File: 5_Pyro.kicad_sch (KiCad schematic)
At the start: 24 parts, among them Q601 IRLZ44N, Q602 IRLZ44N, Q603 IRLZ44N, Q604 IRLZ44N, Q605 IRLZ44N, Q606 IRLZ44N, U601 PC817, U602 PC817, U603 PC817, U604 PC817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

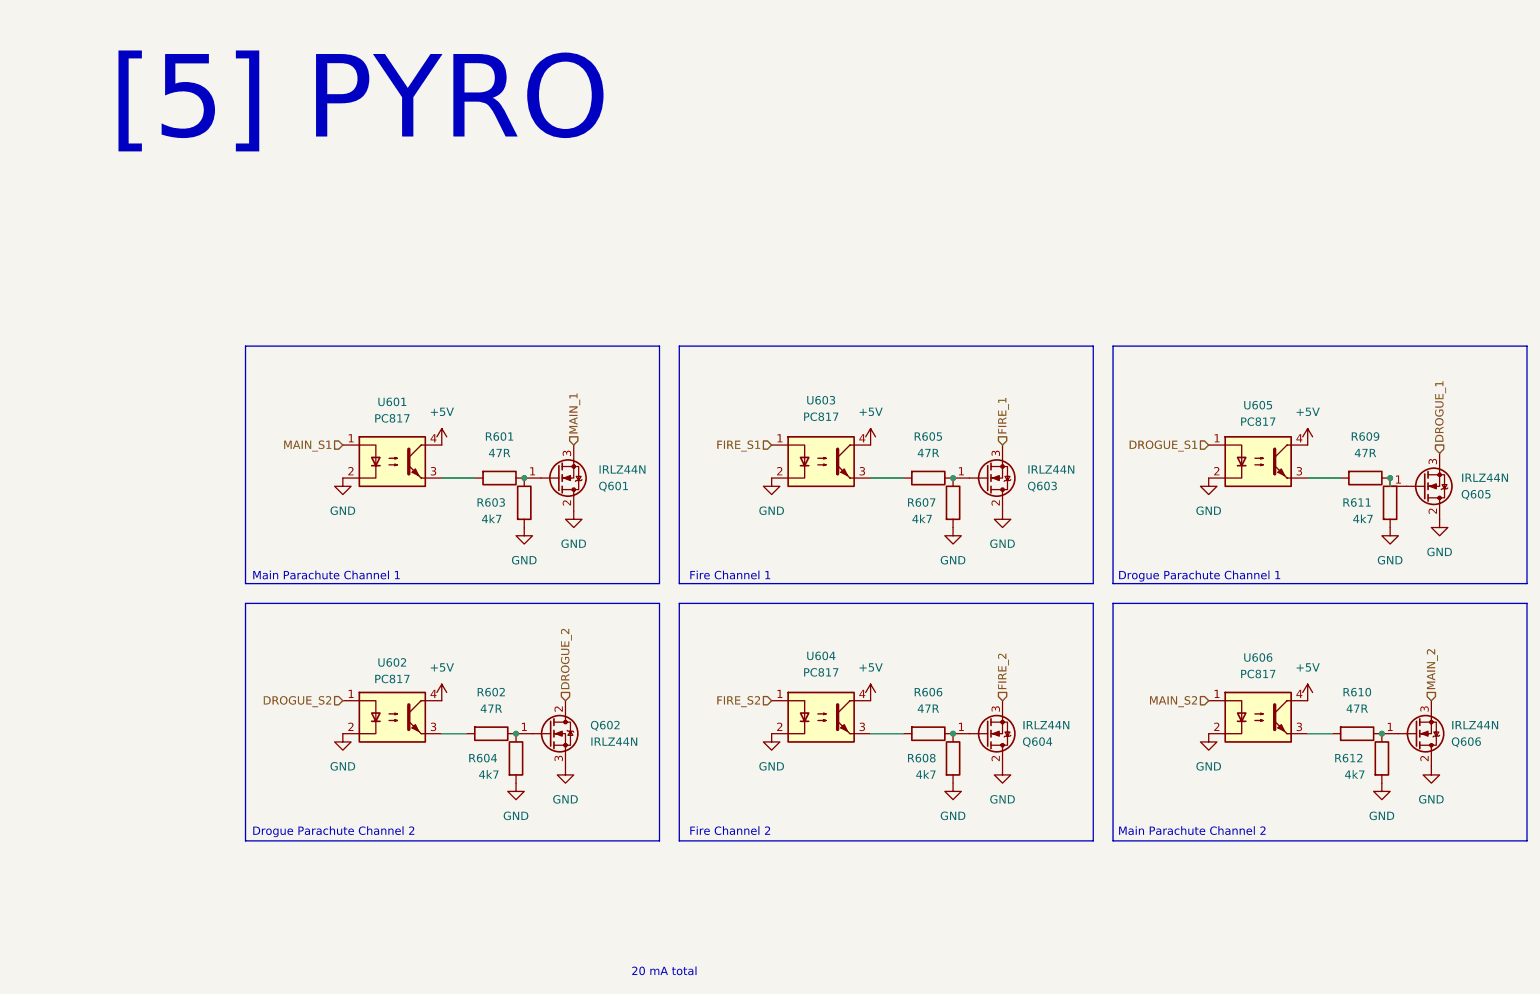
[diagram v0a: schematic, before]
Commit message: Added hardware switch for active control Also added a coupling capacitor between receptacle shells and reference ground Added some more notes
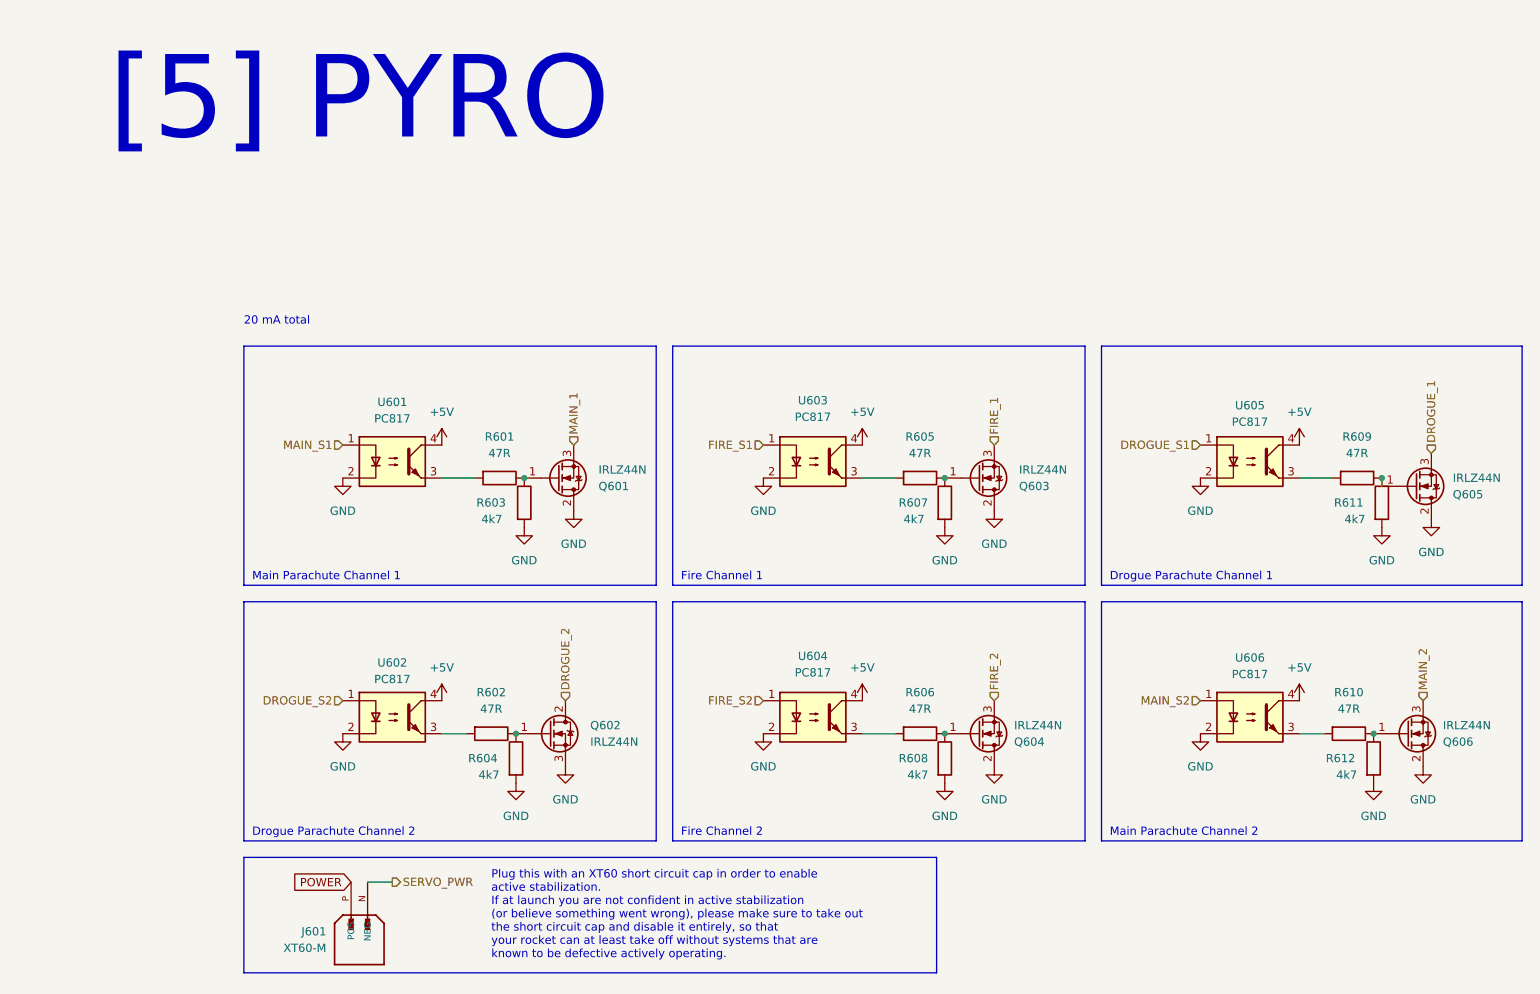
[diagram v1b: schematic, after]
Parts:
- added J601: XT60-M, Connector_AMASS:AMASS_XT60-M_1x02_P7.20mm_Vertical, symbol Polaris_symbols:XT60-M
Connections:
- new net POWER: J601.P (POS)
- new net SERVO_PWR: J601.N (NEG)
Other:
- note added: "Plug this with an XT60 short circuit cap in order to enable active stabilization. If at launch you are not confident in active stabilization (or believe something went wrong), please make sure to take out the short circuit cap and disable it entirely, so that your rocket can at least take off without systems that are known to be defective actively operating."
- title: (none) -> Polaris/Pyro
- moved on the sheet: Q603, Q604, Q605, Q606, R605, R606, R607, R608, R609, R610, R611, R612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

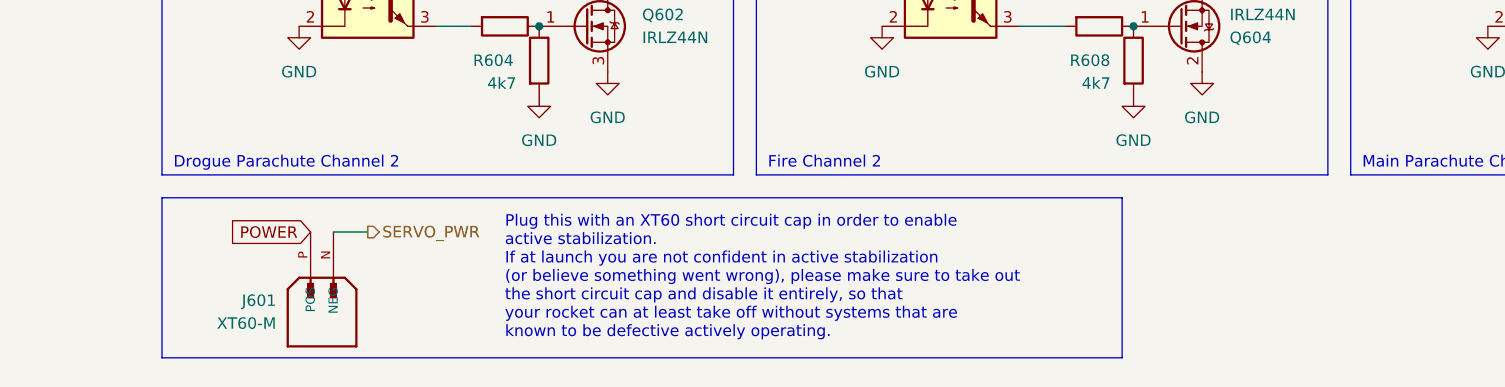
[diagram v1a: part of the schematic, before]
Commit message: Added TVS diode to servo power line
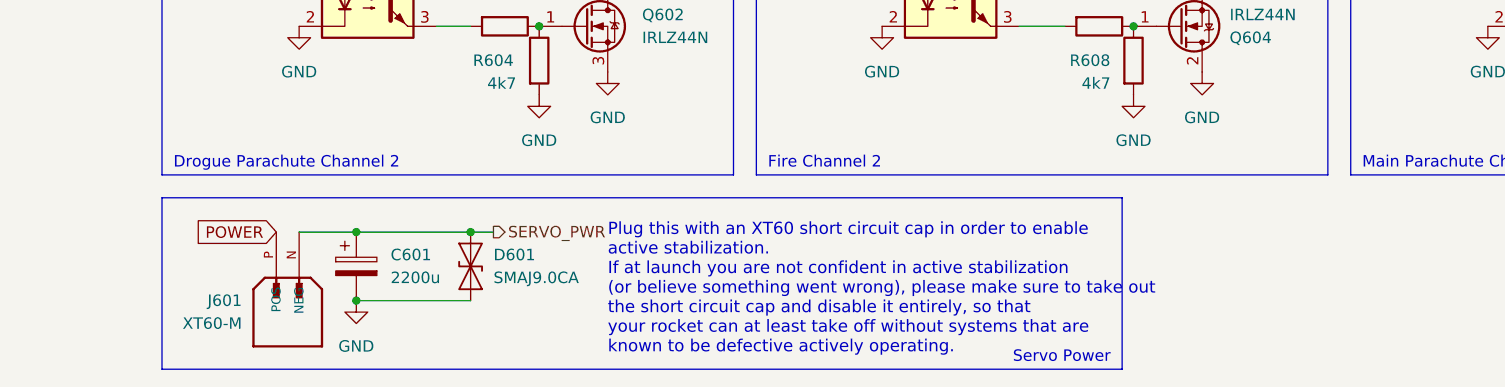
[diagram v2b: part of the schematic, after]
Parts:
- added C601: 2200u, Capacitor_THT:CP_Radial_D13.0mm_P5.00mm, symbol Device:C_Polarized
- added D601: SMAJ9.0CA, Diode_SMD:D_SMA, symbol Diode:SMAJ9.0CA
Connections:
- net GND: now also C601.2, D601.1 (A1)
- net SERVO_PWR: now also C601.1, D601.2 (A2)
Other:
- note added: "Servo Power"
- moved on the sheet: J601

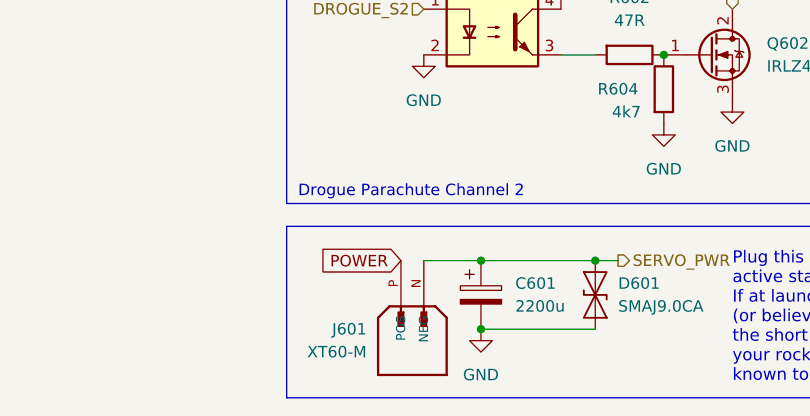
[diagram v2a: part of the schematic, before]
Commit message: Finally started the PCB layout and routing Only took me a few decades Also labeled some unlabeled nets in the schematic Changed the USB mux to be two 1x3 pin headers instead of one 2x3 Edited symbols and footprints to match pin numbers
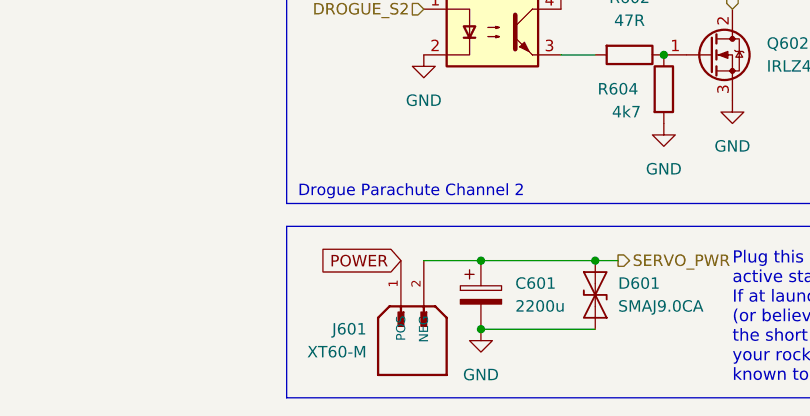
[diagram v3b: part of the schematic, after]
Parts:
- J601: footprint Connector_AMASS:AMASS_XT60-M_1x02_P7.20mm_Vertical -> Connector_AMASS:AMASS_XT60-F_1x02_P7.20mm_Vertical
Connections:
- net POWER: now also J601.1 (POS); no longer J601.P (POS)
- net SERVO_PWR: now also J601.2 (NEG); no longer J601.N (NEG)
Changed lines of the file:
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@@
 			)
 		)
-		(property "Footprint" "Connector_AMASS:AMASS_XT60-M_1x02_P7.20mm_Vertical"
+		(property "Footprint" "Connector_AMASS:AMASS_XT60-F_1x02_P7.20mm_Vertical"
 			(at 58.42 157.48 0)
 			(hide yes)
@@
 			)
 		)
-		(pin "N"
-		)
-		(pin "P"
+		(pin "2"
+		)
+		(pin "1"
 		)
 		(instances
